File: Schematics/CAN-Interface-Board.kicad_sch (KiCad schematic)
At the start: 4 parts, among them J6 Conn_01x05_Pin

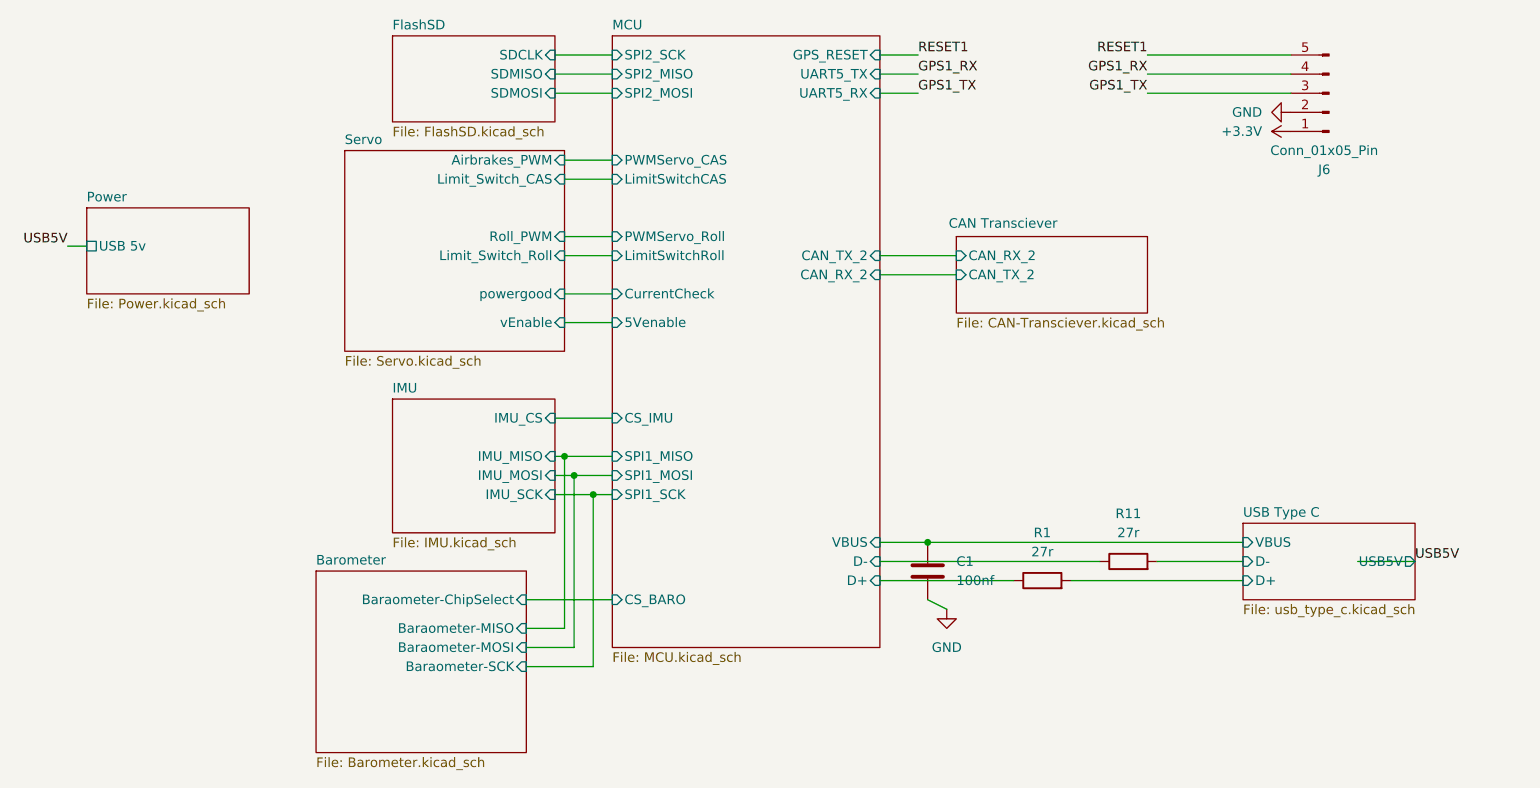
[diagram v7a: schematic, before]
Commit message: Added encoder connection for parafoil motor position information, in buy order ready for purchase
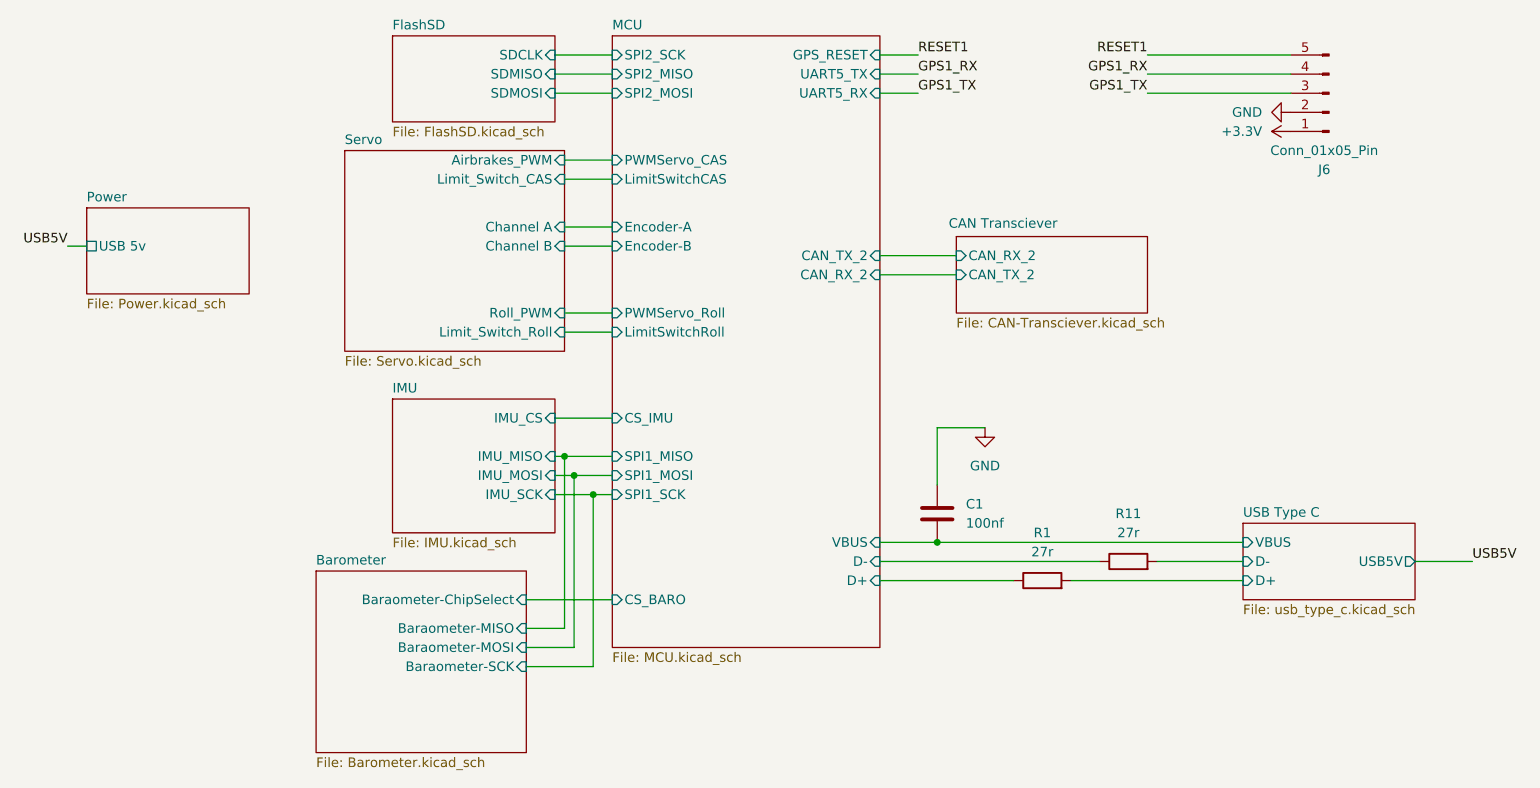
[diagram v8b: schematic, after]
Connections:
- net GND: now also C1.1; no longer C1.2
- net MCU/VBUS: now also C1.2; no longer C1.1
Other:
- sheet MCU ports: added Encoder-A, Encoder-B; removed 5Venable, CurrentCheck
- sheet Servo ports: added Channel A, Channel B; removed powergood, vEnable
- moved on the sheet: C1
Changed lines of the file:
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@@
 	)
 	(junction
-		(at 176.53 127)
+		(at 177.8 127)
 		(diameter 0)
 		(color 0 0 0 0)
@@
 	(wire
 		(pts
+			(xy 184.15 111.76) (xy 177.8 111.76)
+		)
+		(stroke
+			(width 0)
+			(type default)
+		)
+	)
+	(wire
+		(pts
 			(xy 132.08 120.65) (xy 132.08 143.51)
 		)
@@
 	(wire
 		(pts
-			(xy 176.53 127) (xy 218.44 127)
+			(xy 177.8 127) (xy 218.44 127)
 		)
 		(stroke
@@
 	(wire
 		(pts
-			(xy 128.27 88.9) (xy 134.62 88.9)
+			(xy 128.27 99.06) (xy 134.62 99.06)
 		)
 		(stroke
@@
 	(wire
 		(pts
-			(xy 170.18 127) (xy 176.53 127)
+			(xy 170.18 127) (xy 177.8 127)
 		)
 		(stroke
@@
 	(wire
 		(pts
-			(xy 128.27 93.98) (xy 134.62 93.98)
-		)
-		(stroke
-			(width 0)
-			(type default)
-		)
-	)
-	(wire
-		(pts
-			(xy 176.53 134.62) (xy 179.07 135.89)
+			(xy 248.92 129.54) (xy 241.3 129.54)
 		)
 		(stroke
@@
 	(wire
 		(pts
-			(xy 128.27 86.36) (xy 134.62 86.36)
+			(xy 128.27 96.52) (xy 134.62 96.52)
 		)
 		(stroke
@@
 	(wire
 		(pts
-			(xy 233.68 129.54) (xy 241.3 129.54)
-		)
-		(stroke
-			(width 0)
-			(type default)
-		)
-	)
-	(wire
-		(pts
 			(xy 170.18 88.9) (xy 180.34 88.9)
 		)
@@
 	(wire
 		(pts
+			(xy 128.27 85.09) (xy 134.62 85.09)
+		)
+		(stroke
+			(width 0)
+			(type default)
+		)
+	)
+	(wire
+		(pts
 			(xy 187.96 132.08) (xy 170.18 132.08)
 		)
@@
 	(wire
 		(pts
+			(xy 177.8 111.76) (xy 177.8 119.38)
+		)
+		(stroke
+			(width 0)
+			(type default)
+		)
+	)
+	(wire
+		(pts
 			(xy 127 120.65) (xy 132.08 120.65)
 		)
@@
 	(wire
 		(pts
+			(xy 128.27 87.63) (xy 134.62 87.63)
+		)
+		(stroke
+			(width 0)
+			(type default)
+		)
+	)
+	(wire
+		(pts
 			(xy 129.54 118.11) (xy 134.62 118.11)
 		)
@@
 		(pts
 			(xy 123.19 134.62) (xy 134.62 134.62)
-		)
-		(stroke
-			(width 0)
-			(type default)
-		)
-	)
-	(wire
-		(pts
-			(xy 128.27 97.79) (xy 134.62 97.79)
 		)
 		(stroke
@@
 	)
 	(label "USB5V"
-		(at 241.3 129.54 0)
+		(at 248.92 129.54 0)
 		(effects
 			(font
@@
 	(symbol
 		(lib_id "Device:C")
-		(at 176.53 130.81 0)
+		(at 177.8 123.19 0)
 		(unit 1)
 		(body_style 1)
@@
 		(fields_autoplaced yes)
 		(property "Reference" "C1"
-			(at 180.34 129.5399 0)
+			(at 181.61 121.9199 0)
 			(show_name no)
 			(do_not_autoplace no)
@@
 		)
 		(property "Value" "100nf"
-			(at 180.34 132.0799 0)
+			(at 181.61 124.4599 0)
 			(show_name no)
 			(do_not_autoplace no)
@@
 		)
 		(property "Footprint" "Capacitor_SMD:C_0805_2012Metric_Pad1.18x1.45mm_HandSolder"
-			(at 177.4952 134.62 0)
+			(at 178.7652 127 0)
 			(hide yes)
 			(show_name no)
@@
 		)
 		(property "Datasheet" ""
-			(at 176.53 130.81 0)
+			(at 177.8 123.19 0)
 			(hide yes)
 			(show_name no)
@@
 		)
 		(property "Description" ""
-			(at 176.53 130.81 0)
+			(at 177.8 123.19 0)
 			(hide yes)
 			(show_name no)
@@
 		)
 		(property "SnapEDA_Link" ""
-			(at 176.53 130.81 0)
+			(at 177.8 123.19 0)
 			(hide yes)
 			(show_name no)
@@
 		)
 		(property "LCSC" "C49678"
-			(at 176.53 130.81 0)
+			(at 177.8 123.19 0)
 			(hide yes)
 			(show_name no)
@@
 		)
 		(property "DESCRIPTION" ""
-			(at 176.53 130.81 0)
+			(at 177.8 123.19 0)
 			(hide yes)
 			(show_name no)
@@
 	(symbol
 		(lib_id "power:GND")
-		(at 179.07 135.89 0)
+		(at 184.15 111.76 0)
 		(unit 1)
 		(body_style 1)
@@
 		(fields_autoplaced yes)
 		(property "Reference" "#PWR05"
-			(at 179.07 142.24 0)
+			(at 184.15 118.11 0)
 			(hide yes)
 			(show_name no)
@@
 		)
 		(property "Value" "GND"
-			(at 179.07 140.97 0)
+			(at 184.15 116.84 0)
 			(show_name no)
 			(do_not_autoplace no)
@@
 		)
 		(property "Footprint" ""
-			(at 179.07 135.89 0)
+			(at 184.15 111.76 0)
 			(hide yes)
 			(show_name no)
@@
 		)
 		(property "Datasheet" ""
-			(at 179.07 135.89 0)
+			(at 184.15 111.76 0)
 			(hide yes)
 			(show_name no)
@@
 		)
 		(property "Description" "Power symbol creates a global label with name \"GND\" , ground"
-			(at 179.07 135.89 0)
+			(at 184.15 111.76 0)
 			(hide yes)
 			(show_name no)
@@
 		)
 		(pin "Limit_Switch_Roll" input
-			(at 128.27 88.9 0)
-			(effects
-				(font
-					(size 1.27 1.27)
-				)
-				(justify right)
-			)
-		)
-		(pin "powergood" input
-			(at 128.27 93.98 0)
+			(at 128.27 99.06 0)
 			(effects
 				(font
@@
 		)
 		(pin "Roll_PWM" input
-			(at 128.27 86.36 0)
-			(effects
-				(font
-					(size 1.27 1.27)
-				)
-				(justify right)
-			)
-		)
-		(pin "vEnable" input
-			(at 128.27 97.79 0)
+			(at 128.27 96.52 0)
+			(effects
+				(font
+					(size 1.27 1.27)
+				)
+				(justify right)
+			)
+		)
+		(pin "Channel A" input
+			(at 128.27 85.09 0)
+			(effects
+				(font
+					(size 1.27 1.27)
+				)
+				(justify right)
+			)
+		)
+		(pin "Channel B" input
+			(at 128.27 87.63 0)
 			(effects
 				(font
@@
 			)
 		)
-		(pin "5Venable" input
-			(at 134.62 97.79 180)
-			(effects
-				(font
-					(size 1.27 1.27)
-				)
-				(justify left)
-			)
-		)
 		(pin "CAN_RX_2" input
 			(at 170.18 91.44 0)
@@
 		)
 		(pin "PWMServo_Roll" input
-			(at 134.62 86.36 180)
+			(at 134.62 96.52 180)
 			(effects
 				(font
@@
 		)
 		(pin "LimitSwitchRoll" input
-			(at 134.62 88.9 180)
+			(at 134.62 99.06 180)
 			(effects
 				(font
@@
 			)
 		)
-		(pin "CurrentCheck" input
-			(at 134.62 93.98 180)
-			(effects
-				(font
-					(size 1.27 1.27)
-				)
-				(justify left)
-			)
-		)
 		(pin "GPS_RESET" input
 			(at 170.18 62.23 0)
@@
 			)
 		)
+		(pin "Encoder-A" input
+			(at 134.62 85.09 180)
+			(effects
+				(font
+					(size 1.27 1.27)
+				)
+				(justify left)
+			)
+		)
+		(pin "Encoder-B" input
+			(at 134.62 87.63 180)
+			(effects
+				(font
+					(size 1.27 1.27)
+				)
+				(justify left)
+			)
+		)
